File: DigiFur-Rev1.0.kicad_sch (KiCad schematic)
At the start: 32 parts, among them SW1 SW_Push, SW2 SW_Push, SW3 SW_Push, SW4 SW_Push, SW5 MX2A-E1NW, U1 TLV840MADL22DBVR, U2 NL17SZ10DBVT, U3 MCP23017x-x-SO, U4 PCF85063AT, U5 ESP32-C6-DevKitC-1, Y1 ECS-.327-12.5-34QCS-TR

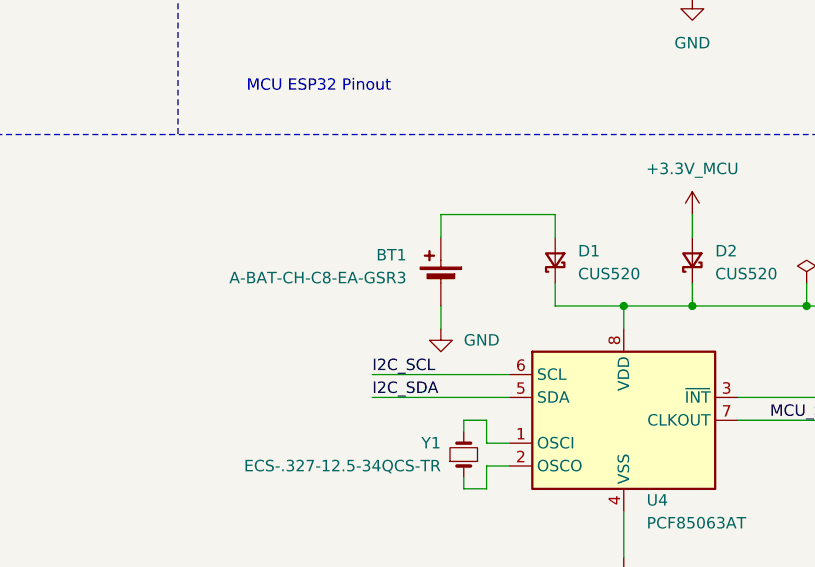
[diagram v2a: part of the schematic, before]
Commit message: Routing completed, silkscreen not yet done.
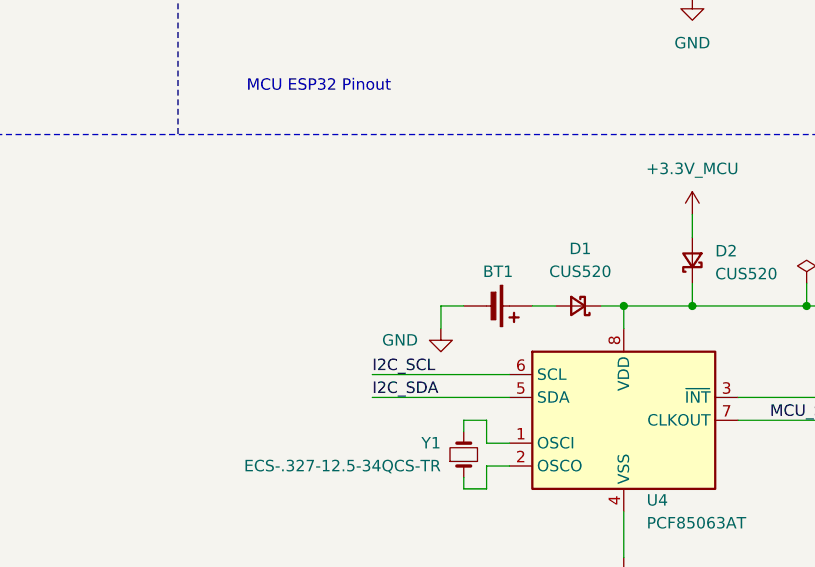
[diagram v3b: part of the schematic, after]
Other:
- moved on the sheet: D1
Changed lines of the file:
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@@
 	)
 	(junction
+		(at 208.28 129.54)
+		(diameter 0)
+		(color 0 0 0 0)
+	)
+	(junction
 		(at 58.42 95.25)
 		(diameter 0)
@@
 	)
 	(junction
-		(at 208.28 129.54)
-		(diameter 0)
-		(color 0 0 0 0)
-	)
-	(junction
 		(at 48.26 69.85)
 		(diameter 0)
@@
 	(wire
 		(pts
-			(xy 187.96 119.38) (xy 187.96 121.92)
-		)
-		(stroke
-			(width 0)
-			(type default)
-		)
-	)
-	(wire
-		(pts
 			(xy 127 36.83) (xy 142.24 36.83)
 		)
@@
 	(wire
 		(pts
-			(xy 200.66 129.54) (xy 208.28 129.54)
+			(xy 205.74 129.54) (xy 208.28 129.54)
 		)
 		(stroke
@@
 	(wire
 		(pts
+			(xy 187.96 129.54) (xy 190.5 129.54)
+		)
+		(stroke
+			(width 0)
+			(type default)
+		)
+	)
+	(wire
+		(pts
 			(xy 58.42 95.25) (xy 68.58 95.25)
 		)
@@
 	(wire
 		(pts
-			(xy 187.96 119.38) (xy 200.66 119.38)
-		)
-		(stroke
-			(width 0)
-			(type default)
-		)
-	)
-	(wire
-		(pts
 			(xy 22.86 148.59) (xy 35.56 148.59)
 		)
@@
 	(wire
 		(pts
-			(xy 200.66 119.38) (xy 200.66 121.92)
-		)
-		(stroke
-			(width 0)
-			(type default)
-		)
-	)
-	(wire
-		(pts
 			(xy 93.98 62.23) (xy 88.9 62.23)
 		)
@@
 	(wire
 		(pts
-			(xy 200.66 127) (xy 200.66 129.54)
-		)
-		(stroke
-			(width 0)
-			(type default)
-		)
-	)
-	(wire
-		(pts
 			(xy 48.26 69.85) (xy 101.6 69.85)
 		)
@@
 	(wire
 		(pts
+			(xy 198.12 129.54) (xy 200.66 129.54)
+		)
+		(stroke
+			(width 0)
+			(type default)
+		)
+	)
+	(wire
+		(pts
 			(xy 48.26 69.85) (xy 48.26 82.55)
 		)
@@
 		)
 		(property "Value" "GND"
-			(at 190.5 133.35 0)
+			(at 185.42 133.35 0)
 			(show_name no)
 			(do_not_autoplace no)
@@
 					(size 1.27 1.27)
 				)
-				(justify right)
+				(justify left)
 			)
 		)
@@
 	)
 	(symbol
-		(lib_id "Device:Battery_Cell")
-		(at 187.96 127 0)
-		(mirror y)
-		(unit 1)
-		(body_style 1)
-		(exclude_from_sim no)
-		(in_bom yes)
-		(on_board yes)
-		(in_pos_files yes)
-		(dnp no)
-		(property "Reference" "BT1"
-			(at 184.15 123.8884 0)
-			(show_name no)
-			(do_not_autoplace no)
-			(effects
-				(font
-					(size 1.27 1.27)
-				)
-				(justify left)
-			)
-		)
-		(property "Value" "A-BAT-CH-C8-EA-GSR3"
-			(at 184.15 126.4284 0)
-			(show_name no)
-			(do_not_autoplace no)
-			(effects
-				(font
-					(size 1.27 1.27)
-				)
-				(justify left)
-			)
-		)
-		(property "Footprint" "Battery:BatteryHolder_Keystone_1060_1x2032"
-			(at 187.96 125.476 90)
-			(hide yes)
-			(show_name no)
-			(do_not_autoplace no)
-			(effects
-				(font
-					(size 1.27 1.27)
-				)
-			)
-		)
-		(property "Datasheet" "https://www.assmann-wsw.com/uploads/datasheets/ASS_9162_CO.pdf"
-			(at 187.96 125.476 90)
-			(hide yes)
-			(show_name no)
-			(do_not_autoplace no)
-			(effects
-				(font
-					(size 1.27 1.27)
-				)
-			)
-		)
-		(property "Description" "Single-cell battery"
-			(at 187.96 127 0)
-			(hide yes)
-			(show_name no)
-			(do_not_autoplace no)
-			(effects
-				(font
-					(size 1.27 1.27)
-				)
-			)
-		)
-		(property "Sim.Device" "V"
-			(at 187.96 127 0)
-			(hide yes)
-			(show_name no)
-			(do_not_autoplace no)
-			(effects
-				(font
-					(size 1.27 1.27)
-				)
-			)
-		)
-		(property "Sim.Type" "DC"
-			(at 187.96 127 0)
-			(hide yes)
-			(show_name no)
-			(do_not_autoplace no)
-			(effects
-				(font
-					(size 1.27 1.27)
-				)
-			)
-		)
-		(property "Sim.Pins" "1=+ 2=-"
-			(at 187.96 127 0)
-			(hide yes)
-			(show_name no)
-			(do_not_autoplace no)
-			(effects
-				(font
-					(size 1.27 1.27)
-				)
-			)
-		)
-		(pin "1"
-		)
-		(pin "2"
-		)
-		(instances
-			(project "DigiFur-Rev1.0"
-				(path "/f34a0579-48a0-44f8-9f4d-f4d692adcf3d"
-					(reference "BT1")
-					(unit 1)
-				)
-			)
-		)
-	)
-	(symbol
 		(lib_id "Device:R_Small")
 		(at 170.18 180.34 0)
@@
 	(symbol
 		(lib_id "Device:D_Schottky_Small")
-		(at 200.66 124.46 90)
+		(at 203.2 129.54 180)
 		(unit 1)
 		(body_style 1)
@@
 		(fields_autoplaced yes)
 		(property "Reference" "D1"
-			(at 203.2 123.4439 90)
+			(at 203.454 123.19 0)
 			(show_name no)
 			(do_not_autoplace no)
@@
 					(size 1.27 1.27)
 				)
-				(justify right)
 			)
 		)
 		(property "Value" "CUS520"
-			(at 203.2 125.9839 90)
+			(at 203.454 125.73 0)
 			(show_name no)
 			(do_not_autoplace no)
@@
 					(size 1.27 1.27)
 				)
-				(justify right)
 			)
 		)
 		(property "Footprint" "Diode_SMD:D_SOD-323_HandSoldering"
-			(at 200.66 124.46 90)
+			(at 203.2 129.54 90)
 			(hide yes)
 			(show_name no)
@@
 		)
 		(property "Datasheet" "https://toshiba.semicon-storage.com/info/CUS520_datasheet_en_20230708.pdf?did=7041&prodName=CUS520"
-			(at 200.66 124.46 90)
+			(at 203.2 129.54 90)
 			(hide yes)
 			(show_name no)
@@
 		)
 		(property "Description" "Schottky diode, small symbol"
-			(at 200.66 124.46 0)
+			(at 203.2 129.54 0)
 			(hide yes)
 			(show_name no)
@@
 					(unit 1)
 				)
+			)
+		)
+	)
+	(symbol
+		(lib_id "Device:Battery_Cell")
+		(at 193.04 129.54 270)
+		(unit 1)
+		(body_style 1)
+		(exclude_from_sim no)
+		(in_bom yes)
+		(on_board yes)
+		(in_pos_files yes)
+		(dnp no)
+		(property "Reference" "BT1"
+			(at 194.31 125.73 90)
+			(show_name no)
+			(do_not_autoplace no)
+			(effects
+				(font
+					(size 1.27 1.27)
+				)
+			)
+		)
+		(property "Value" "A-BAT-CH-C8-EA-GSR3"
+			(at 194.8815 124.46 90)
+			(hide yes)
+			(show_name no)
+			(do_not_autoplace no)
+			(effects
+				(font
+					(size 1.27 1.27)
+				)
+			)
+		)
+		(property "Footprint" "Battery:BatteryHolder_Keystone_1060_1x2032"
+			(at 194.564 129.54 90)
+			(hide yes)
+			(show_name no)
+			(do_not_autoplace no)
+			(effects
+				(font
+					(size 1.27 1.27)
+				)
+			)
+		)
+		(property "Datasheet" "https://www.assmann-wsw.com/uploads/datasheets/ASS_9162_CO.pdf"
+			(at 194.564 129.54 90)
+			(hide yes)
+			(show_name no)
+			(do_not_autoplace no)
+			(effects
+				(font
+					(size 1.27 1.27)
+				)
+			)
+		)
+		(property "Description" "Single-cell battery"
+			(at 193.04 129.54 0)
+			(hide yes)
+			(show_name no)
+			(do_not_autoplace no)
+			(effects
+				(font
+					(size 1.27 1.27)
+				)
+			)
+		)
+		(property "Sim.Device" "V"
+			(at 193.04 129.54 0)
+			(hide yes)
+			(show_name no)
+			(do_not_autoplace no)
+			(effects
+				(font
+					(size 1.27 1.27)
+				)
+			)
+		)
+		(property "Sim.Type" "DC"
+			(at 193.04 129.54 0)
+			(hide yes)
+			(show_name no)
+			(do_not_autoplace no)
+			(effects
+				(font
+					(size 1.27 1.27)
+				)
+			)
+		)
+		(property "Sim.Pins" "1=+ 2=-"
+			(at 193.04 129.54 0)
+			(hide yes)
+			(show_name no)
+			(do_not_autoplace no)
+			(effects
+				(font
+					(size 1.27 1.27)
+				)
+			)
+		)
+		(pin "2"
+		)
+		(pin "1"
+		)
+		(instances
+			(project "DigiFur-Rev1.0"
+				(path "/f34a0579-48a0-44f8-9f4d-f4d692adcf3d"
+					(reference "BT1")
+					(unit 1)
+				)

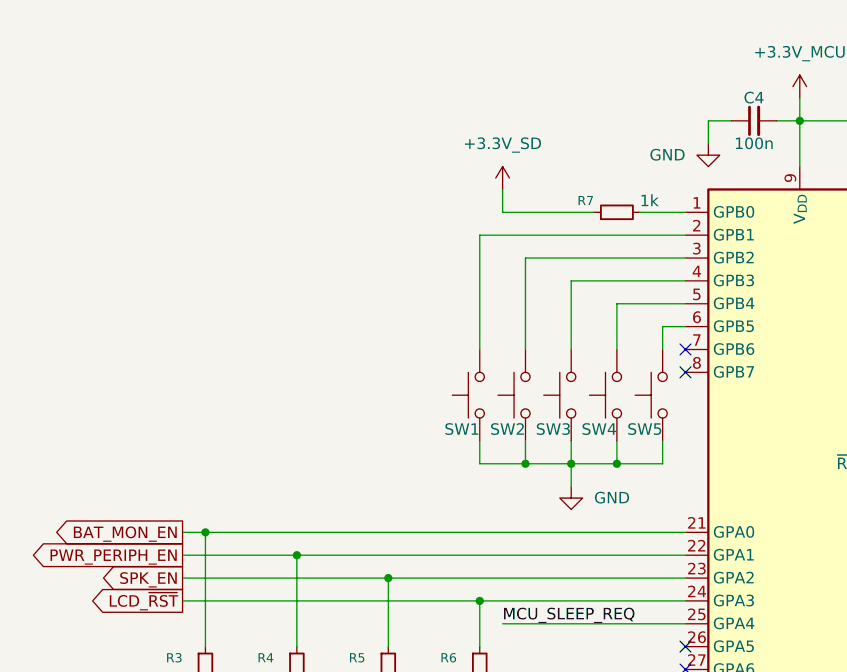
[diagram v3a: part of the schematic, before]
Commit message: Updated pairing button.
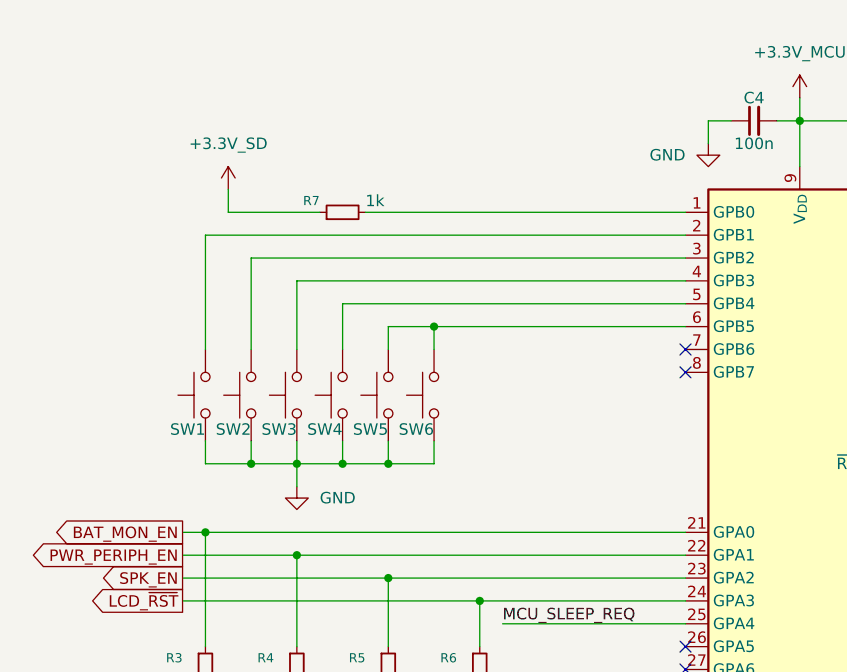
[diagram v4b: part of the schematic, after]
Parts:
- added SW6: SW_Push, Button_Switch_THT:SW_PUSH-12mm_Wuerth-430476085716, symbol Switch:SW_Push
- SW5: footprint Button_Switch_Keyboard:SW_Cherry_MX_1.00u_PCB -> Button_Switch_Keyboard:SW_Cherry_MX_2.75u_PCB
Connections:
- net GND: now also SW6.2
- net at SW5.1, U3.6 (GPB5): now also SW6.1
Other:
- moved on the sheet: R7, SW1, SW2, SW3, SW4, SW5

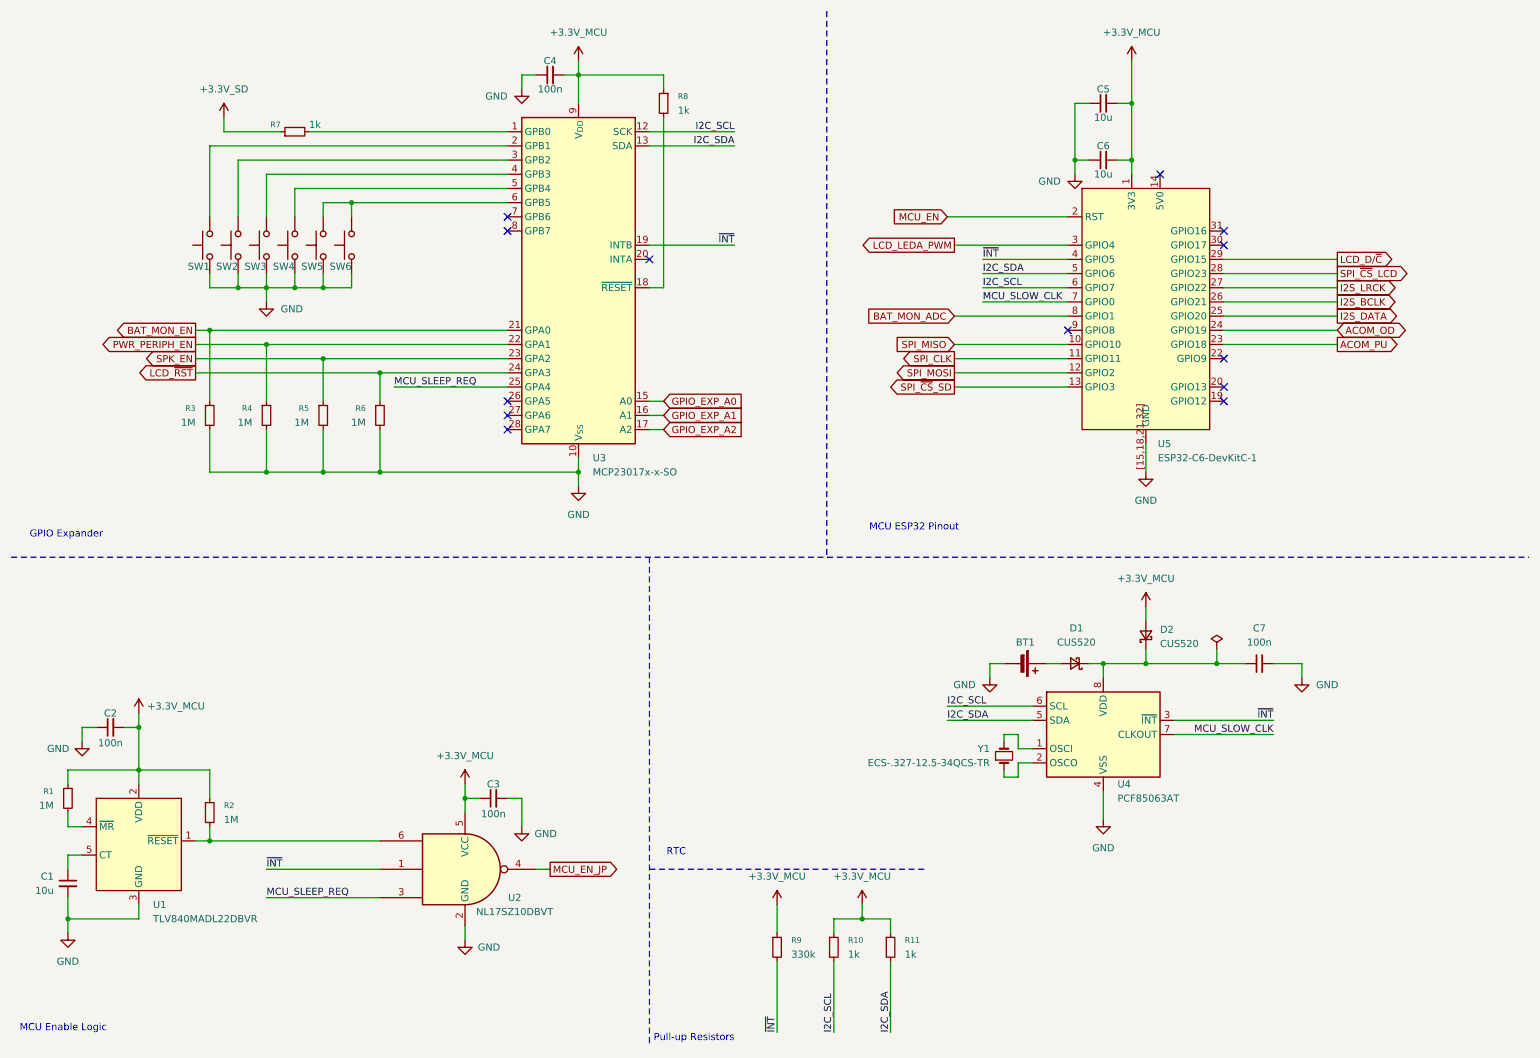
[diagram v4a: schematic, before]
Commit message: Revision to fix problems from first board fab
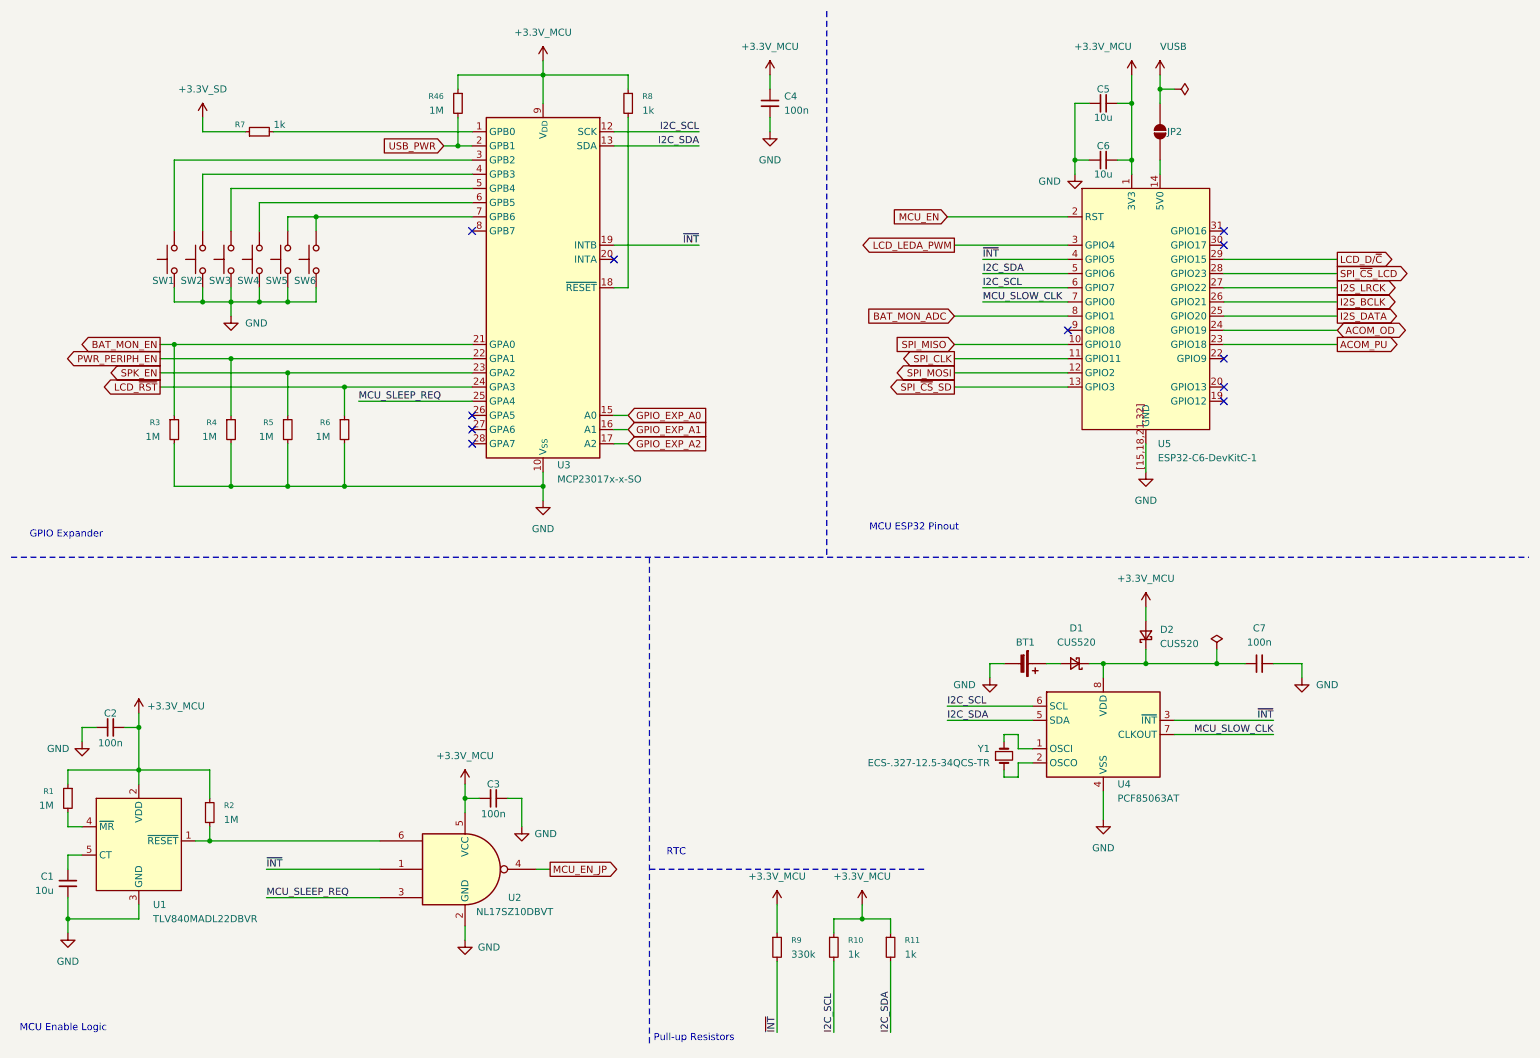
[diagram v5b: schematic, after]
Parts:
- added JP2: SolderJumper_2_Open, Jumper:SolderJumper-2_P1.3mm_Open_TrianglePad1.0x1.5mm, symbol Jumper:SolderJumper_2_Open
- added R46: 1M, Resistor_SMD:R_0603_1608Metric_Pad0.98x0.95mm_HandSolder, symbol Device:R_Small
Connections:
- net +3.3V_MCU: now also C4.1, R46.1; no longer C4.2
- net GND: now also C4.2; no longer C4.1
- net at U5.14 (5V0): now also JP2.2 (B)
- net at SW5.1, SW6.1: now also U3.7 (GPB6); no longer U3.6 (GPB5)
- net at SW1.1: now also U3.3 (GPB2); no longer U3.2 (GPB1)
- net at SW2.1: now also U3.4 (GPB3); no longer U3.3 (GPB2)
- net at SW3.1: now also U3.5 (GPB4); no longer U3.4 (GPB3)
- net at SW4.1: now also U3.6 (GPB5); no longer U3.5 (GPB4)
- new net USB_PWR: R46.2, U3.2 (GPB1)
- new net VUSB: JP2.1 (A)
- no-connect marks 13 -> 11
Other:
- moved on the sheet: R3, R4, R5, R6, R7, R8, SW1, SW2, SW3, SW4, SW5, SW6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
